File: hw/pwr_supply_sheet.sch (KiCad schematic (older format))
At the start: 15 parts

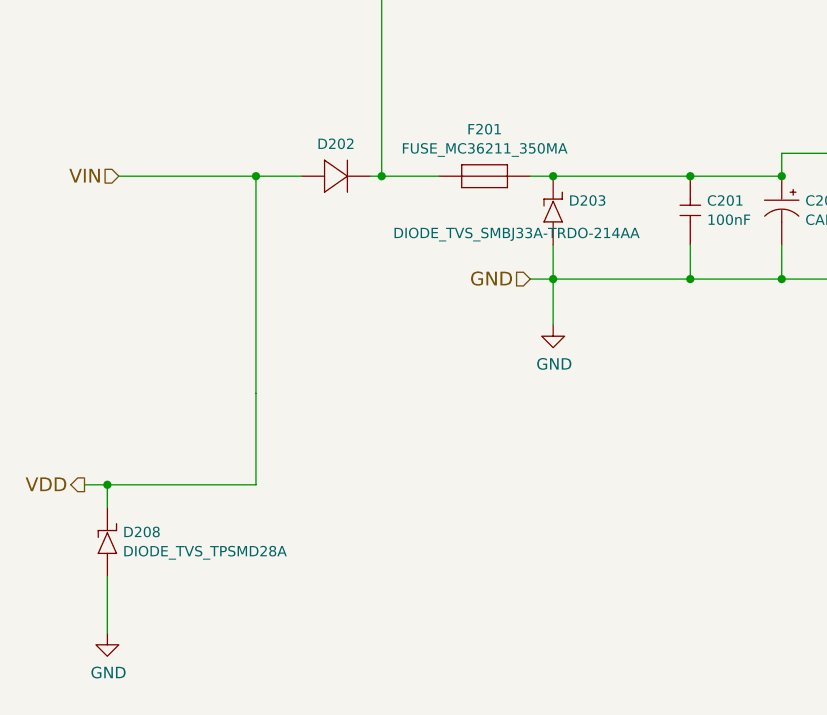
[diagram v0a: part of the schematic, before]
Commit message: 4.1.0 pcb ordered, with modified flyback diodes
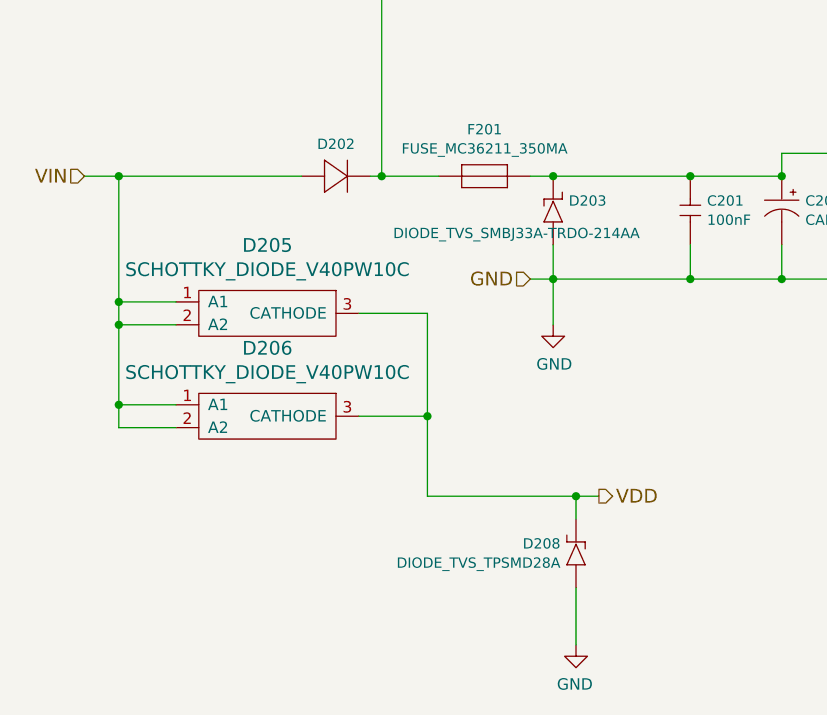
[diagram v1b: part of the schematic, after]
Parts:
- added D205, D206: SCHOTTKY_DIODE_V40PW10C, usevolt:SlimDPAK, symbol fsb-rescue:SCHOTTKY_DIODE_V40PW10C
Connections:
- net VDD: now also D205.3 (CATHODE), D206.3 (CATHODE); no longer D202.P$1 (P)
- new net VIN: D202.P$1 (P), D205.1 (A1), D205.2 (A2), D206.1 (A1), D206.2 (A2)
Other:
- moved on the sheet: D208
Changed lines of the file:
@@
 Comment4 ""
 $EndDescr
-Text HLabel 900  3850 0    60   Input ~ 0
+Text HLabel 750  3850 0    60   Input ~ 0
 VIN
 $Comp
@@
 $EndComp
 Wire Wire Line
-	900  3850 1500 3850
-Wire Wire Line
 	3800 3750 4550 3750
 Text HLabel 7050 3600 2    60   Output ~ 0
@@
 Wire Wire Line
 	8750 3600 8600 3600
-Text HLabel 750  5200 0    60   Output ~ 0
+Text HLabel 3000 5250 2    60   Output ~ 0
 VDD
 Text HLabel 2700 4300 0    60   Input ~ 0
@@
 	3800 3850 3800 3750
 Wire Wire Line
-	750  5200 850  5200
-Connection ~ 1500 3850
+	3000 5250 2900 5250
 Wire Wire Line
 	2700 3850 2800 3850
@@
 VBAT_SENSE
 Wire Wire Line
-	1500 4800 1500 3850
-Wire Wire Line
 	1800 1850 2150 1850
 Wire Wire Line
@@
 L fsb-rescue:DIODE_TVS_TPSMD28A D208
 U 1 1 5A0E2A07
-P 850 5500
-F 0 "D208" V 942 5432 45  0000 R CNN
-F 1 "DIODE_TVS_TPSMD28A" V 858 5432 45  0000 R CNN
-F 2 "usevolt:DO-214AB" H 880 5650 20  0001 C CNN
-F 3 "http://www.littelfuse.com/~/media/electronics/datasheets/tvs_diodes/littelfuse_tvs_diode_tpsmd_datasheet.pdf.pdf" H 960 5510 60  0001 C CNN
-F 4 "Digi-Key" H 1260 5810 60  0001 C CNN "1st Source"
-F 5 "Littlefuse" H 1060 5610 60  0001 C CNN "Manufacturer"
-F 6 "TPSMD28A" H 1160 5710 60  0001 C CNN "Manufacturer Part Number"
-F 7 "F6570CT-ND" H 1360 5910 60  0001 C CNN "1st Source Part Number"
-	1    850  5500
-	0    -1   -1   0
-$EndComp
-Wire Wire Line
-	850  5300 850  5200
-Connection ~ 850  5200
+P 2900 5550
+F 0 "D208" V 2992 5482 45  0000 R CNN
+F 1 "DIODE_TVS_TPSMD28A" V 2908 5482 45  0000 R CNN
+F 2 "usevolt:DO-214AB" H 2930 5700 20  0001 C CNN
+F 3 "http://www.littelfuse.com/~/media/electronics/datasheets/tvs_diodes/littelfuse_tvs_diode_tpsmd_datasheet.pdf.pdf" H 3010 5560 60  0001 C CNN
+F 4 "Digi-Key" H 3310 5860 60  0001 C CNN "1st Source"
+F 5 "Littlefuse" H 3110 5660 60  0001 C CNN "Manufacturer"
+F 6 "TPSMD28A" H 3210 5760 60  0001 C CNN "Manufacturer Part Number"
+F 7 "F6570CT-ND" H 3410 5960 60  0001 C CNN "1st Source Part Number"
+	1    2900 5550
+	0    1    -1   0
+$EndComp
+Wire Wire Line
+	2900 5350 2900 5250
+Connection ~ 2900 5250
 $Comp
 L fsb-rescue:GND #PWR0201
 U 1 1 5A0E2B45
-P 850 5850
-F 0 "#PWR0201" H 850 5600 50  0001 C CNN
-F 1 "GND" H 855 5677 50  0000 C CNN
-F 2 "" H 850 5850 50  0000 C CNN
-F 3 "" H 850 5850 50  0000 C CNN
-	1    850  5850
-	1    0    0    -1
-$EndComp
-Wire Wire Line
-	850  5850 850  5600
+P 2900 5900
+F 0 "#PWR0201" H 2900 5650 50  0001 C CNN
+F 1 "GND" H 2905 5727 50  0000 C CNN
+F 2 "" H 2900 5900 50  0000 C CNN
+F 3 "" H 2900 5900 50  0000 C CNN
+	1    2900 5900
+	-1   0    0    -1
+$EndComp
+Wire Wire Line
+	2900 5900 2900 5650
 $Comp
 L fsb-rescue:DIODE_TVS_SMBJ33A-TRDO-214AA D203
@@
 	2800 4300 3400 4300
 Wire Wire Line
-	1500 3850 1700 3850
-Wire Wire Line
 	2050 3850 2300 3850
 Wire Wire Line
@@
 	1800 1300 1800 1650
 Wire Wire Line
-	850  5200 1500 5200
-Wire Wire Line
-	1500 5200 1500 4800
+	2900 5250 2250 5250
+Wire Wire Line
+	750  3850 900  3850
+$Comp
+L fsb-rescue:SCHOTTKY_DIODE_V40PW10C D206
+U 1 1 5B19508D
+P 1550 4950
+F 0 "D206" H 1550 5297 60  0000 C CNN
+F 1 "SCHOTTKY_DIODE_V40PW10C" H 1550 5191 60  0000 C CNN
+F 2 "usevolt:SlimDPAK" H 1350 4600 60  0001 C CNN
+F 3 "http://www.farnell.com/datasheets/2245239.pdf?_ga=2.16591231.874534928.1505194133-1862443086.1504075057" H 1350 4600 60  0001 C CNN
+F 4 "2535169" H 1900 5550 60  0001 C CNN "1st Source Part Number"
+F 5 "Digikey" H 2000 5650 60  0001 C CNN "2nd Source"
+F 6 "Farnell" H 1800 5450 60  0001 C CNN "1st Source"
+F 7 "V40PW10CHM3/I" H 1700 5350 60  0001 C CNN "Manufacturer Part Number"
+F 8 "V40PW10CHM3/IGICT-ND" H 2100 5750 60  0001 C CNN "2nd Source Part Number"
+F 9 "VISHAY" H 1600 5250 60  0001 C CNN "Manufacturer"
+	1    1550 4950
+	1    0    0    -1
+$EndComp
+$Comp
+L fsb-rescue:SCHOTTKY_DIODE_V40PW10C D205
+U 1 1 5B195179
+P 1550 4500
+F 0 "D205" H 1550 4847 60  0000 C CNN
+F 1 "SCHOTTKY_DIODE_V40PW10C" H 1550 4741 60  0000 C CNN
+F 2 "usevolt:SlimDPAK" H 1350 4150 60  0001 C CNN
+F 3 "http://www.farnell.com/datasheets/2245239.pdf?_ga=2.16591231.874534928.1505194133-1862443086.1504075057" H 1350 4150 60  0001 C CNN
+F 4 "2535169" H 1900 5100 60  0001 C CNN "1st Source Part Number"
+F 5 "Digikey" H 2000 5200 60  0001 C CNN "2nd Source"
+F 6 "Farnell" H 1800 5000 60  0001 C CNN "1st Source"
+F 7 "V40PW10CHM3/I" H 1700 4900 60  0001 C CNN "Manufacturer Part Number"
+F 8 "V40PW10CHM3/IGICT-ND" H 2100 5300 60  0001 C CNN "2nd Source Part Number"
+F 9 "VISHAY" H 1600 4800 60  0001 C CNN "Manufacturer"
+	1    1550 4500
+	1    0    0    -1
+$EndComp
+Wire Wire Line
+	1950 4450 2250 4450
+Wire Wire Line
+	2250 4450 2250 4900
+Wire Wire Line
+	1950 4900 2250 4900
+Connection ~ 2250 4900
+Wire Wire Line
+	2250 4900 2250 5250
+Wire Wire Line
+	1150 4400 900  4400
+Wire Wire Line
+	900  4400 900  3850
+Connection ~ 900  3850
+Wire Wire Line
+	900  3850 1700 3850
+Wire Wire Line
+	1150 4500 900  4500
+Wire Wire Line
+	900  4500 900  4400
+Connection ~ 900  4400
+Wire Wire Line
+	1150 4850 900  4850
+Wire Wire Line
+	900  4850 900  4500
+Connection ~ 900  4500
+Wire Wire Line
+	1150 4950 900  4950
+Wire Wire Line
+	900  4950 900  4850
+Connection ~ 900  4850
 $EndSCHEMATC

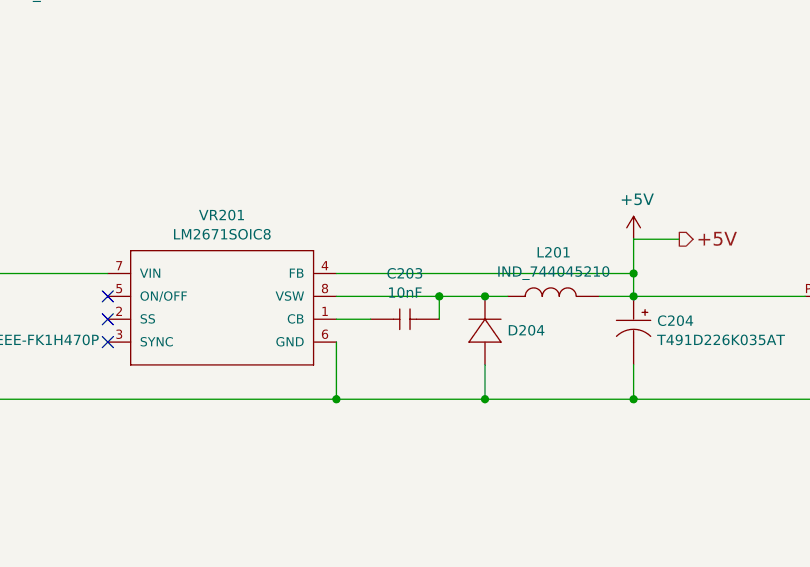
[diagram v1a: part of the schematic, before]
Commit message: HAL updated to latest uv bootloader, starting to draw 6.0.0 pcb
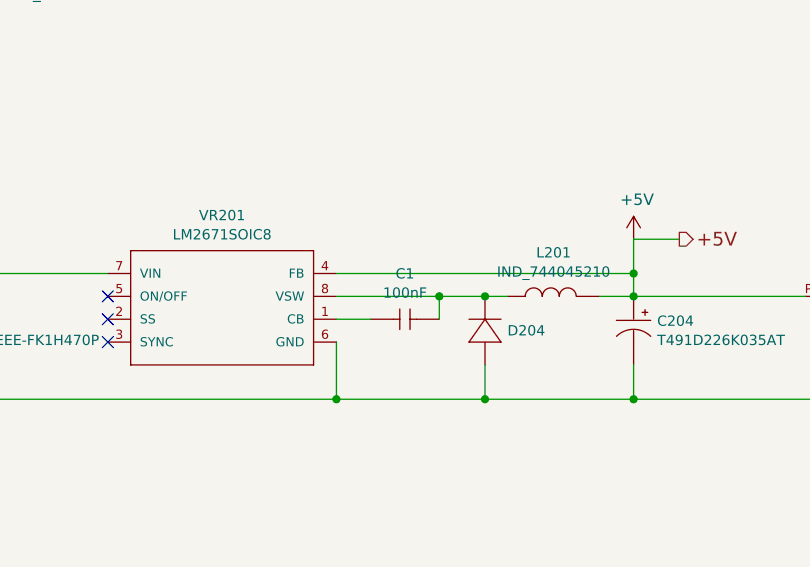
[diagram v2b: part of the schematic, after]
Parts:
- removed C203: 10nF, kemet:0603, symbol fsb-rescue:10nF
- added C1: 100nF, kemet:0603, symbol fsb-rescue:100nF
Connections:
- net at VR201.1 (CB): now also C1.1 (C1)
- net at D204.P$2 (N), L201.1, VR201.8 (VSW): now also C1.2 (C2)
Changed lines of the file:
@@
-$EndComp
-$Comp
-L fsb-rescue:10nF C203
-U 1 1 57B822C5
-P 5800 3950
-F 0 "C203" H 5850 4149 45  0000 C CNN
-F 1 "10nF" H 5850 4065 45  0000 C CNN
-F 2 "kemet:0603" H 5830 4100 20  0001 C CNN
-F 3 "http://www.farnell.com/datasheets/2064086.pdf?_ga=1.250530118.1948984246.1460023966" H 5704 3959 60  0001 C CNN
-F 4 "1457729" H 6104 4359 60  0001 C CNN "1st Source Part Number"
-F 5 "C0603C103J3GACTU" H 5904 4159 60  0001 C CNN "Manufacturer Part Number"
-F 6 "Farnell" H 6004 4259 60  0001 C CNN "1st Source"
-F 7 "KEMET" H 5804 4059 60  0001 C CNN "Manufacturer"
-	1    5800 3950
-	1    0    0    -1
 $EndComp
 $Comp
@@
 	900  4950 900  4850
 Connection ~ 900  4850
+$Comp
+L fsb-rescue:100nF C1
+U 1 1 5C021329
+P 5800 3950
+F 0 "C1" H 5850 4149 45  0000 C CNN
+F 1 "100nF" H 5850 4065 45  0000 C CNN
+F 2 "kemet:0603" H 5830 4100 20  0001 C CNN
+F 3 "http://www.farnell.com/datasheets/2062872.pdf?_ga=1.250530118.1948984246.1460023966" H 5704 3959 60  0001 C CNN
+F 4 "1288255" H 6104 4359 60  0001 C CNN "1st Source Part Number"
+F 5 "C0603C104K5RACTU" H 5904 4159 60  0001 C CNN "Manufacturer Part Number"
+F 6 "Farnell" H 6004 4259 60  0001 C CNN "1st Source"
+F 7 "KEMET" H 5804 4059 60  0001 C CNN "Manufacturer"
+	1    5800 3950
+	1    0    0    -1
+$EndComp
 $EndSCHEMATC

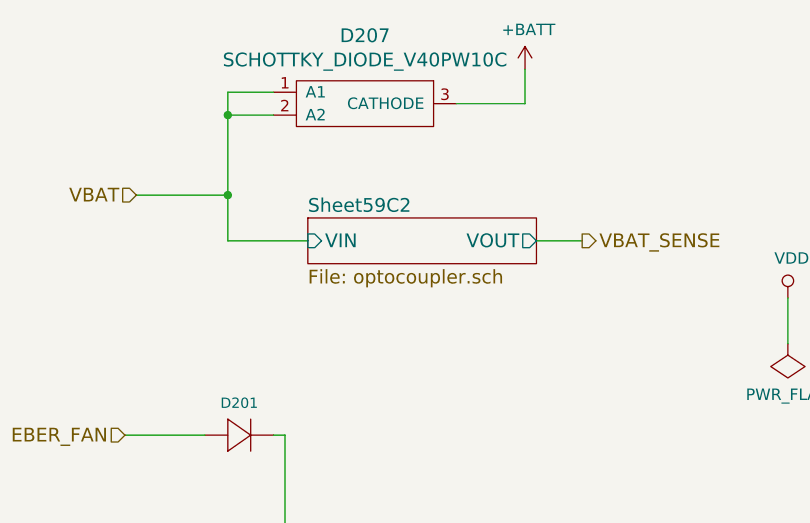
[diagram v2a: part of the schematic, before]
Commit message: hw 6.0.0 created, fits uw aluminium enclosure
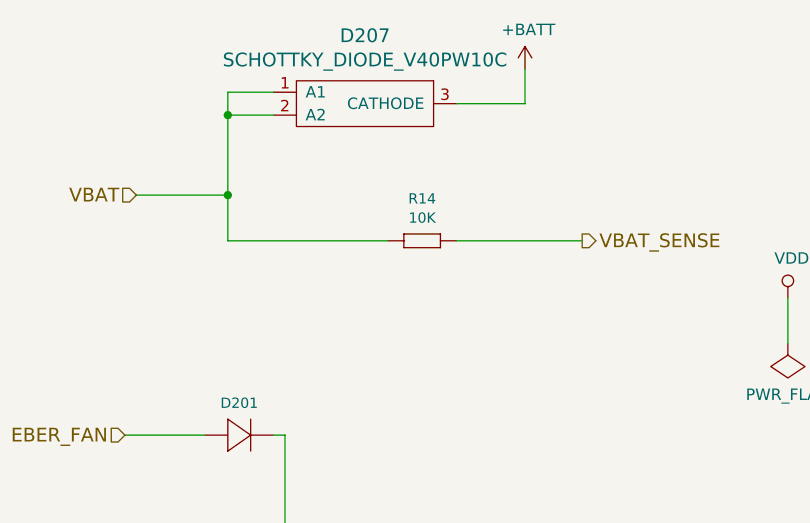
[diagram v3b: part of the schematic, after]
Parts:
- added R14: 10K, yageo:0603, symbol fsb-rescue:10K
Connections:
- net VBAT: now also R14.2 (R2)
- net VBAT_SENSE: now also R14.1 (R1)
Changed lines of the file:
@@
 Text HLabel 3350 1850 2    60   Output ~ 0
 VBAT_SENSE
-Wire Wire Line
-	1800 1850 2150 1850
-Wire Wire Line
-	3150 1850 3350 1850
 $Comp
 L fsb-rescue:LM2671SOIC8 VR201
@@
 	1    0    0    -1
 $EndComp
-$Sheet
-S 2150 1750 1000 200
-U 59C2BC93
-F0 "Sheet59C2" 60
-F1 "optocoupler.sch" 60
-F2 "VOUT" O R 3150 1850 60
-F3 "VIN" I L 2150 1850 60
-$EndSheet
 $Comp
 L fsb-rescue:SCHOTTKY_DIODE_V40PW10C D207
@@
 	1    0    0    -1
 $EndComp
+$Comp
+L fsb-rescue:10K R14
+U 1 1 5C513F03
+P 2600 1850
+F 0 "R14" H 2650 2034 45  0000 C CNN
+F 1 "10K" H 2650 1950 45  0000 C CNN
+F 2 "yageo:0603" H 2630 2000 20  0001 C CNN
+F 3 "" H 2569 1889 60  0001 C CNN
+F 4 "Digikey" H 2869 2189 60  0001 C CNN "1st Source"
+F 5 "RC0603FR-0710KL" H 2769 2089 60  0001 C CNN "Manufacturer Part Number"
+F 6 "YAGEO" H 2669 1989 60  0001 C CNN "Manufacturer"
+	1    2600 1850
+	1    0    0    -1
+$EndComp
+Wire Wire Line
+	1800 1850 2500 1850
+Wire Wire Line
+	2800 1850 3350 1850
 $EndSCHEMATC
